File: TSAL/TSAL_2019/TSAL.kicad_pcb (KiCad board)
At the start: 2 copper layers, 68.6 x 68.6 mm, 53 parts, among them J1 Main Connector, U1 L7805, U2 LM555, U3 SN754410

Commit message: TSAL Schematic done
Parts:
- removed C3, C5: CP, Capacitors_THT:C_Disc_D3.0mm_W1.6mm_P2.50mm
- removed C4: 10uF, Capacitors_THT:CP_Radial_D5.0mm_P2.50mm
- removed U2: LM555, Housings_DIP:DIP-8_W7.62mm
- removed U3: SN754410, Housings_DIP:DIP-16_W7.62mm
- added D31: LR A67F-U2AB-1-1-30-R33-Z, FSFootprints:LED_SMD-2, F.Cu at (151.4, 58.5)
- added D32: LR A67F-U2AB-1-1-30-R33-Z, FSFootprints:LED_SMD-2, F.Cu at (151.4, 63.8)
- added D33: LR A67F-U2AB-1-1-30-R33-Z, FSFootprints:LED_SMD-2, F.Cu at (156.1, 58.5)
- added D34: LR A67F-U2AB-1-1-30-R33-Z, FSFootprints:LED_SMD-2, F.Cu at (151.4, 69.0)
- added D35: LR A67F-U2AB-1-1-30-R33-Z, FSFootprints:LED_SMD-2, F.Cu at (160.9, 58.5)
- added D36: LR A67F-U2AB-1-1-30-R33-Z, FSFootprints:LED_SMD-2, F.Cu at (156.1, 63.8)
- added D37: LR A67F-U2AB-1-1-30-R33-Z, FSFootprints:LED_SMD-2, F.Cu at (151.4, 74.3)
- added D38: LR A67F-U2AB-1-1-30-R33-Z, FSFootprints:LED_SMD-2, F.Cu at (160.9, 63.8)
- added D39: LR A67F-U2AB-1-1-30-R33-Z, FSFootprints:LED_SMD-2, F.Cu at (156.1, 69.0)
- added D40: LR A67F-U2AB-1-1-30-R33-Z, FSFootprints:LED_SMD-2, F.Cu at (165.6, 58.5)
- added D41: LR A67F-U2AB-1-1-30-R33-Z, FSFootprints:LED_SMD-2, F.Cu at (170.4, 58.5)
- added D42: LR A67F-U2AB-1-1-30-R33-Z, FSFootprints:LED_SMD-2, F.Cu at (165.6, 63.8)
- added D43: LR A67F-U2AB-1-1-30-R33-Z, FSFootprints:LED_SMD-2, F.Cu at (160.9, 69.0)
- added D44: LR A67F-U2AB-1-1-30-R33-Z, FSFootprints:LED_SMD-2, F.Cu at (156.1, 74.3)
- added D45: LR A67F-U2AB-1-1-30-R33-Z, FSFootprints:LED_SMD-2, F.Cu at (170.4, 63.8)
- added D46: LR A67F-U2AB-1-1-30-R33-Z, FSFootprints:LED_SMD-2, F.Cu at (175.1, 58.5)
- added D47: LR A67F-U2AB-1-1-30-R33-Z, FSFootprints:LED_SMD-2, F.Cu at (165.6, 69.0)
- added D48: LR A67F-U2AB-1-1-30-R33-Z, FSFootprints:LED_SMD-2, F.Cu at (160.9, 74.3)
- added D49: LR A67F-U2AB-1-1-30-R33-Z, FSFootprints:LED_SMD-2, F.Cu at (170.4, 69.0)
- added D50: LR A67F-U2AB-1-1-30-R33-Z, FSFootprints:LED_SMD-2, F.Cu at (179.9, 58.5)
- added D51: LR A67F-U2AB-1-1-30-R33-Z, FSFootprints:LED_SMD-2, F.Cu at (175.1, 63.8)
- added D52: LR A67F-U2AB-1-1-30-R33-Z, FSFootprints:LED_SMD-2, F.Cu at (165.6, 74.3)
- added D53: LR A67F-U2AB-1-1-30-R33-Z, FSFootprints:LED_SMD-2, F.Cu at (170.4, 74.3)
- added D54: LR A67F-U2AB-1-1-30-R33-Z, FSFootprints:LED_SMD-2, F.Cu at (179.9, 63.8)
- added D55: LR A67F-U2AB-1-1-30-R33-Z, FSFootprints:LED_SMD-2, F.Cu at (175.1, 69.0)
- added D56: LR A67F-U2AB-1-1-30-R33-Z, FSFootprints:LED_SMD-2, F.Cu at (184.6, 58.5)
- added D57: LR A67F-U2AB-1-1-30-R33-Z, FSFootprints:LED_SMD-2, F.Cu at (184.6, 63.8)
- added D58: LR A67F-U2AB-1-1-30-R33-Z, FSFootprints:LED_SMD-2, F.Cu at (179.9, 69.0)
- added D59: LR A67F-U2AB-1-1-30-R33-Z, FSFootprints:LED_SMD-2, F.Cu at (175.1, 74.3)
- added D60: LR A67F-U2AB-1-1-30-R33-Z, FSFootprints:LED_SMD-2, F.Cu at (184.6, 69.0)
- added Q1: TSM320N03CX, TO_SOT_Packages_SMD:SOT-23, F.Cu at (183.6, 71.0)
- added Q2: TSM320N03CX, TO_SOT_Packages_SMD:SOT-23, F.Cu at (196.8, 68.6)
- added Q3: TSM320N03CX, TO_SOT_Packages_SMD:SOT-23, F.Cu at (182.3, 74.7)
- added Q4: TSM320N03CX, TO_SOT_Packages_SMD:SOT-23, F.Cu at (178.9, 74.7)
- added R10: 120, Resistors_SMD:R_0805_HandSoldering, F.Cu at (174.8, 68.3)
- added R11: 120, Resistors_SMD:R_0805_HandSoldering, F.Cu at (170.0, 72.0)
- added R12: 120, Resistors_SMD:R_0805_HandSoldering, F.Cu at (174.8, 70.1)
- added R13: 120, Resistors_SMD:R_0805_HandSoldering, F.Cu at (170.0, 73.9)
- added R14: 120, Resistors_SMD:R_0805_HandSoldering, F.Cu at (179.5, 72.0)
- added R15: 120, Resistors_SMD:R_0805_HandSoldering, F.Cu at (179.5, 68.3)
- added R16: 120, Resistors_SMD:R_0805_HandSoldering, F.Cu at (170.0, 75.8)
- added R17: 120, Resistors_SMD:R_0805_HandSoldering, F.Cu at (174.8, 72.0)
- added R18: 1k, Resistors_SMD:R_0805_HandSoldering, F.Cu at (200.5, 79.7)
- added R19: 100k, Resistors_SMD:R_0805_HandSoldering, F.Cu at (200.5, 81.6)
- added R20: 68, Resistors_SMD:R_0805_HandSoldering, F.Cu at (179.5, 70.1)
- added R21: 68, Resistors_SMD:R_0805_HandSoldering, F.Cu at (174.8, 73.9)
- added R22: 68, Resistors_SMD:R_0805_HandSoldering, F.Cu at (170.0, 77.7)
- added R23: 68, Resistors_SMD:R_0805_HandSoldering, F.Cu at (184.3, 68.3)
- added R24: 68, Resistors_SMD:R_0805_HandSoldering, F.Cu at (174.8, 75.8)
- added R25: 68, Resistors_SMD:R_0805_HandSoldering, F.Cu at (170.0, 68.3)
- added R26: 1k, Resistors_SMD:R_0805_HandSoldering, F.Cu at (205.2, 79.7)
- added R27: 100k, Resistors_SMD:R_0805_HandSoldering, F.Cu at (205.2, 81.6)
- added R9: 120, Resistors_SMD:R_0805_HandSoldering, F.Cu at (170.0, 70.1)
- C1: footprint Capacitors_THT:CP_Radial_D5.0mm_P2.50mm -> Capacitors_SMD:C_0805_HandSoldering
- C2: value CP -> 30uF; footprint Capacitors_THT:CP_Radial_D5.0mm_P2.50mm -> Capacitors_SMD:CP_Elec_5x5.3
- D1, D10, D11, D12, D13, D14, D15, D16, D17, D18, D19, D2, D20, D21, D22, D23, D24, D25, D26, D27, D28, D29, D3, D30, D4, D5, D6, D7, D8, D9: value Led_Small -> LT A6SG-V2AB-35-Z
- J1: footprint Connectors_Molex:Molex_NanoFit_2x02x2.50mm_Straight -> Connectors_Molex:Molex_NanoFit_1x04x2.50mm_Angled
- R1: value 15K -> 10k
- R2: value 15K -> 1k
- R3: value 68 -> 5k
- R4, R5: value 68 -> 1k
- R6, R7: value 68 -> 100k
- R8: value 68 -> 120
- U1: value L7805 -> SE555; footprint TO_SOT_Packages_THT:TO-220-3_Horizontal -> Housings_SOIC:SOIC-8_3.9x4.9mm_Pitch1.27mm
- moved U1 24.1 mm to (106.7, 116.8)
- moved LS1 5.20 mm to (138.6, 101.6)
- moved LS2 5.08 mm to (166.4, 101.6)
- moved J1 3.59 mm to (156.2, 124.5), turned to 180 degrees
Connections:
- C1 pad 1: /12V -> GND
- C1 pad 2: /GND -> Net-(C1-Pad2)
- C2 pad 1: /5V -> Net-(C2-Pad1)
- C2 pad 2: /GND -> GND
- D1 pad 2: /OSC -> +12V
- D10 pad 2: Net-(D10-Pad2) -> +12V
- D11 pad 2: /OSC -> Net-(D10-Pad1)
- D13 pad 2: Net-(D12-Pad1) -> +12V
- D16 pad 2: /OSC -> +12V
- D19 pad 2: Net-(D18-Pad1) -> +12V
- D21 pad 2: /OSC -> Net-(D20-Pad1)
- D22 pad 2: Net-(D21-Pad1) -> +12V
- D25 pad 2: Net-(D24-Pad1) -> +12V
- D26 pad 2: /OSC -> Net-(D25-Pad1)
- D28 pad 2: Net-(D27-Pad1) -> +12V
- D4 pad 2: Net-(D3-Pad1) -> +12V
- D6 pad 2: /OSC -> Net-(D5-Pad1)
- D7 pad 2: Net-(D6-Pad1) -> +12V
- D9 pad 1: Net-(D10-Pad2) -> Net-(D9-Pad1)
- J1 pad 1: /12V -> +12V
- J1 pad 2: /SIG_TSAL -> SIG_TSAL
- J1 pad 3: /SIG_RTDS -> SIG_RTDS
- J1 pad 4: /GND -> GND
- LS1 pad 1: /RTDS_H -> +12V
- LS1 pad 2: /GND -> Net-(LS1-Pad2)
- LS2 pad 1: /RTDS_H -> +12V
- LS2 pad 2: /GND -> Net-(LS1-Pad2)
- R1 pad 1: /5V -> +12V
- R1 pad 2: Net-(R1-Pad2) -> Net-(Q2-Pad2)
- R2 pad 1: Net-(R1-Pad2) -> +12V
- R2 pad 2: Net-(C4-Pad1) -> Net-(R2-Pad2)
- R3 pad 1: Net-(D5-Pad1) -> Net-(R2-Pad2)
- R3 pad 2: /GND -> Net-(C2-Pad1)
- R4 pad 1: Net-(D10-Pad1) -> SIG_RTDS
- R4 pad 2: /GND -> Net-(Q1-Pad1)
- R5 pad 1: Net-(D15-Pad1) -> SIG_TSAL
- R5 pad 2: /GND -> Net-(Q2-Pad1)
- R6 pad 1: Net-(D20-Pad1) -> Net-(Q1-Pad1)
- R6 pad 2: /GND -> GND
- R7 pad 1: Net-(D25-Pad1) -> Net-(Q2-Pad1)
- R7 pad 2: /GND -> GND
- R8 pad 1: Net-(D30-Pad1) -> Net-(D3-Pad1)
- R8 pad 2: /GND -> Net-(Q3-Pad2)
- U1 pad 1: /12V -> GND
- U1 pad 2: /GND -> Net-(C2-Pad1)
- U1 pad 3: /5V -> 555
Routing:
- net /OSC: track 173.1 -> 0.00 mm
- net /GND: track 75.6 -> 0.00 mm, vias 8 -> 0
- net /RTDS_H: track 68.6 -> 0.00 mm
- net /5V: track 58.9 -> 0.00 mm
- net /SIG_TSAL: track 57.5 -> 0.00 mm
- net /12V: track 54.3 -> 0.00 mm
- net /SIG_RTDS: track 48.6 -> 0.00 mm
- net Net-(U2-Pad3): track 30.3 -> 0.00 mm
- net Net-(C4-Pad1): track 23.8 -> 0.00 mm
- net Net-(R1-Pad2): track 5.18 -> 0.00 mm
- net Net-(D6-Pad1): track 4.20 -> 0.00 mm
- net Net-(D21-Pad1): track 4.20 -> 0.00 mm
- net Net-(D29-Pad1): track 4.19 -> 0.00 mm
- net Net-(D17-Pad1): track 4.19 -> 0.00 mm
- net Net-(D2-Pad1): track 4.19 -> 0.00 mm
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- removed copper zone on B.Cu, net /GND
- removed copper zone on F.Cu, net /GND

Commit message: Finish layout of TSAL 2019 (ugly edition)
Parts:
- D31, D32, D33, D34, D35, D36, D37, D38, D39, D40, D41, D42, D43, D44, D45, D46, D47, D48, D49, D50, D51, D52, D53, D54, D55, D56, D57, D58, D59, D60, R1, R20, R21, R22, R23, R24, R25: moved to B.Cu
- J1: footprint Connectors_Molex:Molex_NanoFit_1x04x2.50mm_Angled -> Connector_Molex:Molex_Nano-Fit_105310-xx04_2x02_P2.50mm_Vertical
- moved D50 81.3 mm to (132.0, 124.3), turned to 228 degrees
- moved D51 74.6 mm to (137.2, 128.0), turned to 240 degrees
- moved R23 73.8 mm to (133.9, 122.2), turned to 138 degrees
- moved D54 72.4 mm to (155.6, 131.9), turned to 276 degrees
- moved D56 71.5 mm to (167.6, 128.0), turned to 300 degrees
- moved R18 69.5 mm to (145.5, 122.2), turned to 90 degrees
- moved D46 68.5 mm to (121.9, 101.6), turned to 180 degrees
- moved D49 66.1 mm to (127.7, 119.5), turned to 216 degrees
- moved R27 65.9 mm to (141.4, 97.7), turned to 180 degrees
- moved R10 65.8 mm to (149.6, 129.0), turned to 354 degrees
- moved R19 65.5 mm to (141.0, 108.8), turned to 90 degrees
- moved Q2 65.0 mm to (144.8, 107.4), turned to 180 degrees
- moved D55 63.0 mm to (161.8, 130.6), turned to 288 degrees
- moved R11 61.8 mm to (133.9, 122.2), turned to 318 degrees
- moved R12 61.8 mm to (125.5, 107.4), turned to 282 degrees
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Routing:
- net +12V: track 0.00 -> 305.1 mm, vias 0 -> 6
- net Net-(Q3-Pad2): track 0.00 -> 168.6 mm
- net Net-(Q4-Pad2): track 0.00 -> 145.4 mm, vias 0 -> 1
- net GND: track 0.00 -> 64.2 mm, vias 0 -> 2
- net Net-(Q3-Pad1): track 0.00 -> 23.6 mm, vias 0 -> 2
- net Net-(C2-Pad1): track 0.00 -> 19.2 mm
- net Net-(Q2-Pad2): track 0.00 -> 19.0 mm, vias 0 -> 2
- net SIG_RTDS: track 0.00 -> 18.7 mm
- net Net-(LS1-Pad2): track 0.00 -> 15.7 mm
- net Net-(Q2-Pad1): track 0.00 -> 13.2 mm
- net Net-(Q4-Pad1): track 0.00 -> 12.8 mm
- net SIG_TSAL: track 0.00 -> 11.2 mm
- net Net-(R2-Pad2): track 0.00 -> 11.2 mm
- net 555: track 0.00 -> 5.70 mm, vias 0 -> 2
- net Net-(Q1-Pad1): track 0.00 -> 4.77 mm
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
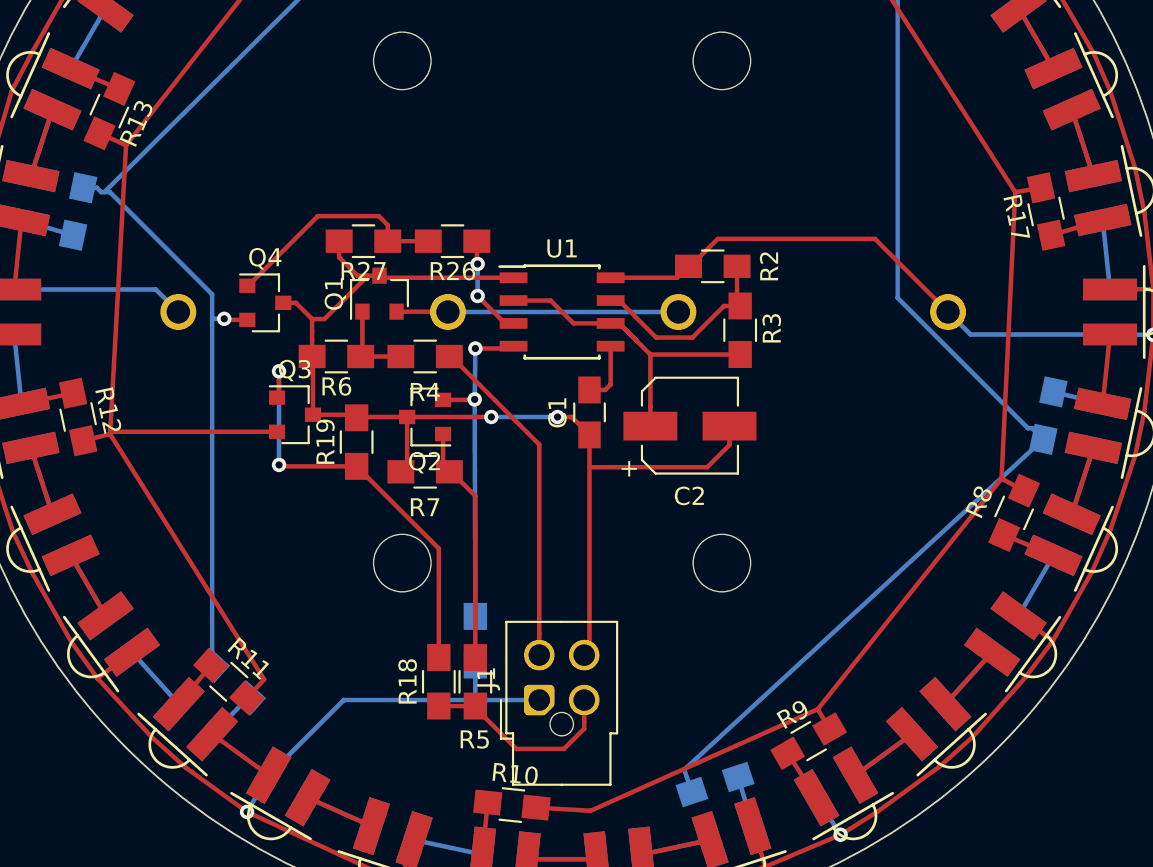
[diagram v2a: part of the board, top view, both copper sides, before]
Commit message: Fix TSAL layout to be less garbage
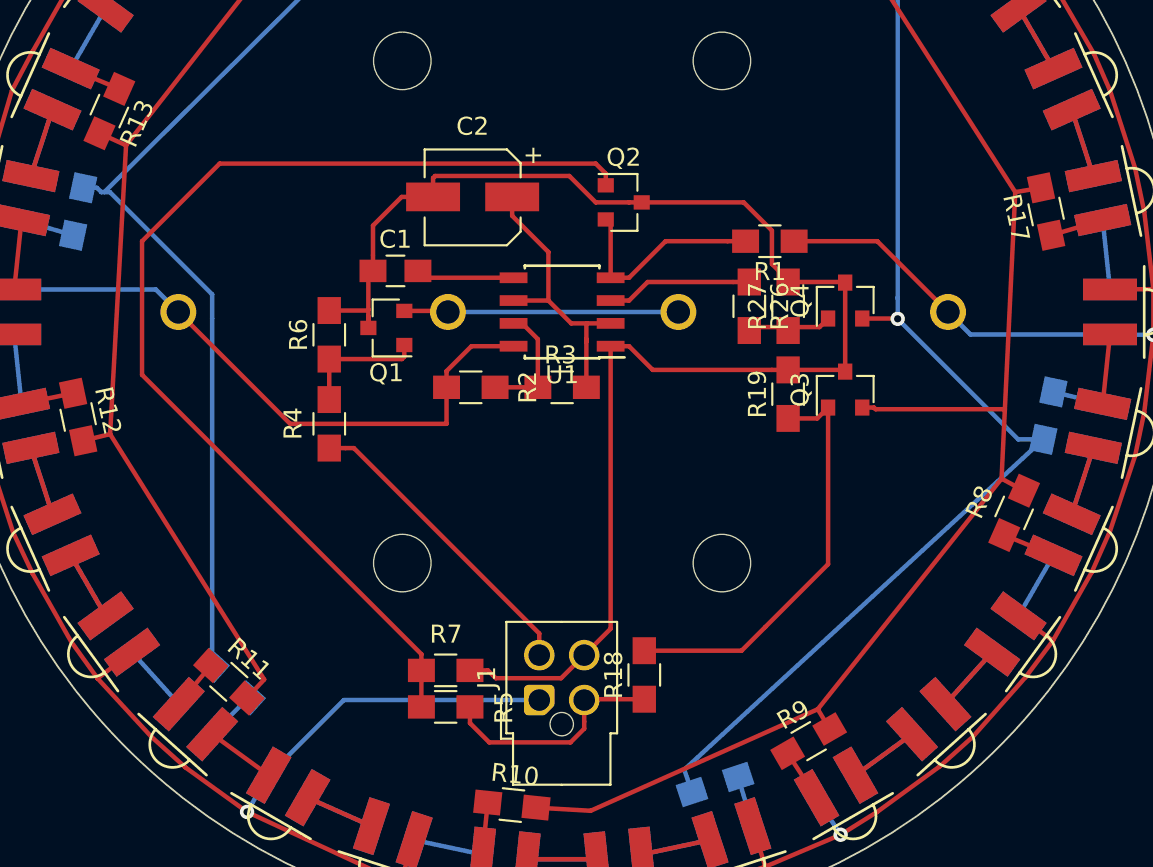
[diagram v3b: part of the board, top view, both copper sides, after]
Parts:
- R1: moved to F.Cu
- moved Q4 32.3 mm to (168.1, 101.0), turned to 90 degrees
- moved Q3 30.6 mm to (168.1, 105.9), turned to 90 degrees
- moved R1 27.6 mm to (164.0, 97.7), turned to 180 degrees
- moved R19 24.2 mm to (165.0, 106.2)
- moved R27 23.9 mm to (165.0, 101.3), turned to 90 degrees
- moved C2 17.6 mm to (147.4, 95.2), turned to 180 degrees
- moved R26 16.9 mm to (162.8, 101.3), turned to 270 degrees
- moved Q2 16.3 mm to (155.8, 95.5), turned to 0 degrees
- moved R2 15.1 mm to (147.3, 105.8)
- moved C1 13.4 mm to (143.1, 99.3), turned to 0 degrees
- moved R18 11.4 mm to (157.0, 121.8)
- moved R7 11.1 mm to (145.9, 121.5), turned to 0 degrees
- moved R3 10.4 mm to (152.4, 105.8), turned to 0 degrees
- moved R4 6.52 mm to (139.4, 107.8), turned to 90 degrees
- moved R5 2.16 mm to (145.9, 123.6), turned to 180 degrees
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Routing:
- net Net-(Q2-Pad1): track 13.2 -> 60.8 mm
- net GND: track 64.2 -> 84.1 mm, vias 2 -> 0
- net +12V: track 305.1 -> 316.7 mm
- net Net-(Q4-Pad1): track 12.8 -> 4.58 mm
- net Net-(Q2-Pad2): track 19.0 -> 12.2 mm, vias 2 -> 0
- net Net-(R2-Pad2): track 11.2 -> 6.77 mm
- net Net-(C2-Pad1): track 19.2 -> 16.7 mm
- net Net-(Q1-Pad1): track 4.77 -> 7.23 mm
- net 555: track 5.70 -> 8.14 mm, vias 2 -> 0
- net Net-(C1-Pad2): track 3.43 -> 5.48 mm
- net SIG_TSAL: track 11.2 -> 13.0 mm
- net SIG_RTDS: track 18.7 -> 17.2 mm
- net Net-(Q3-Pad2): track 168.6 -> 167.2 mm
- net Net-(Q4-Pad2): track 145.4 -> 146.1 mm
- net Net-(Q3-Pad1): track 23.6 -> 23.4 mm, vias 2 -> 0
